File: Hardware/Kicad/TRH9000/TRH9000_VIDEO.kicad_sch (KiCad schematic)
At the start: 34 parts, among them J2 S-Video, J3 Composite, J4 DB15_Female_HighDensity, Q1 BC817, U6 CXA2075M

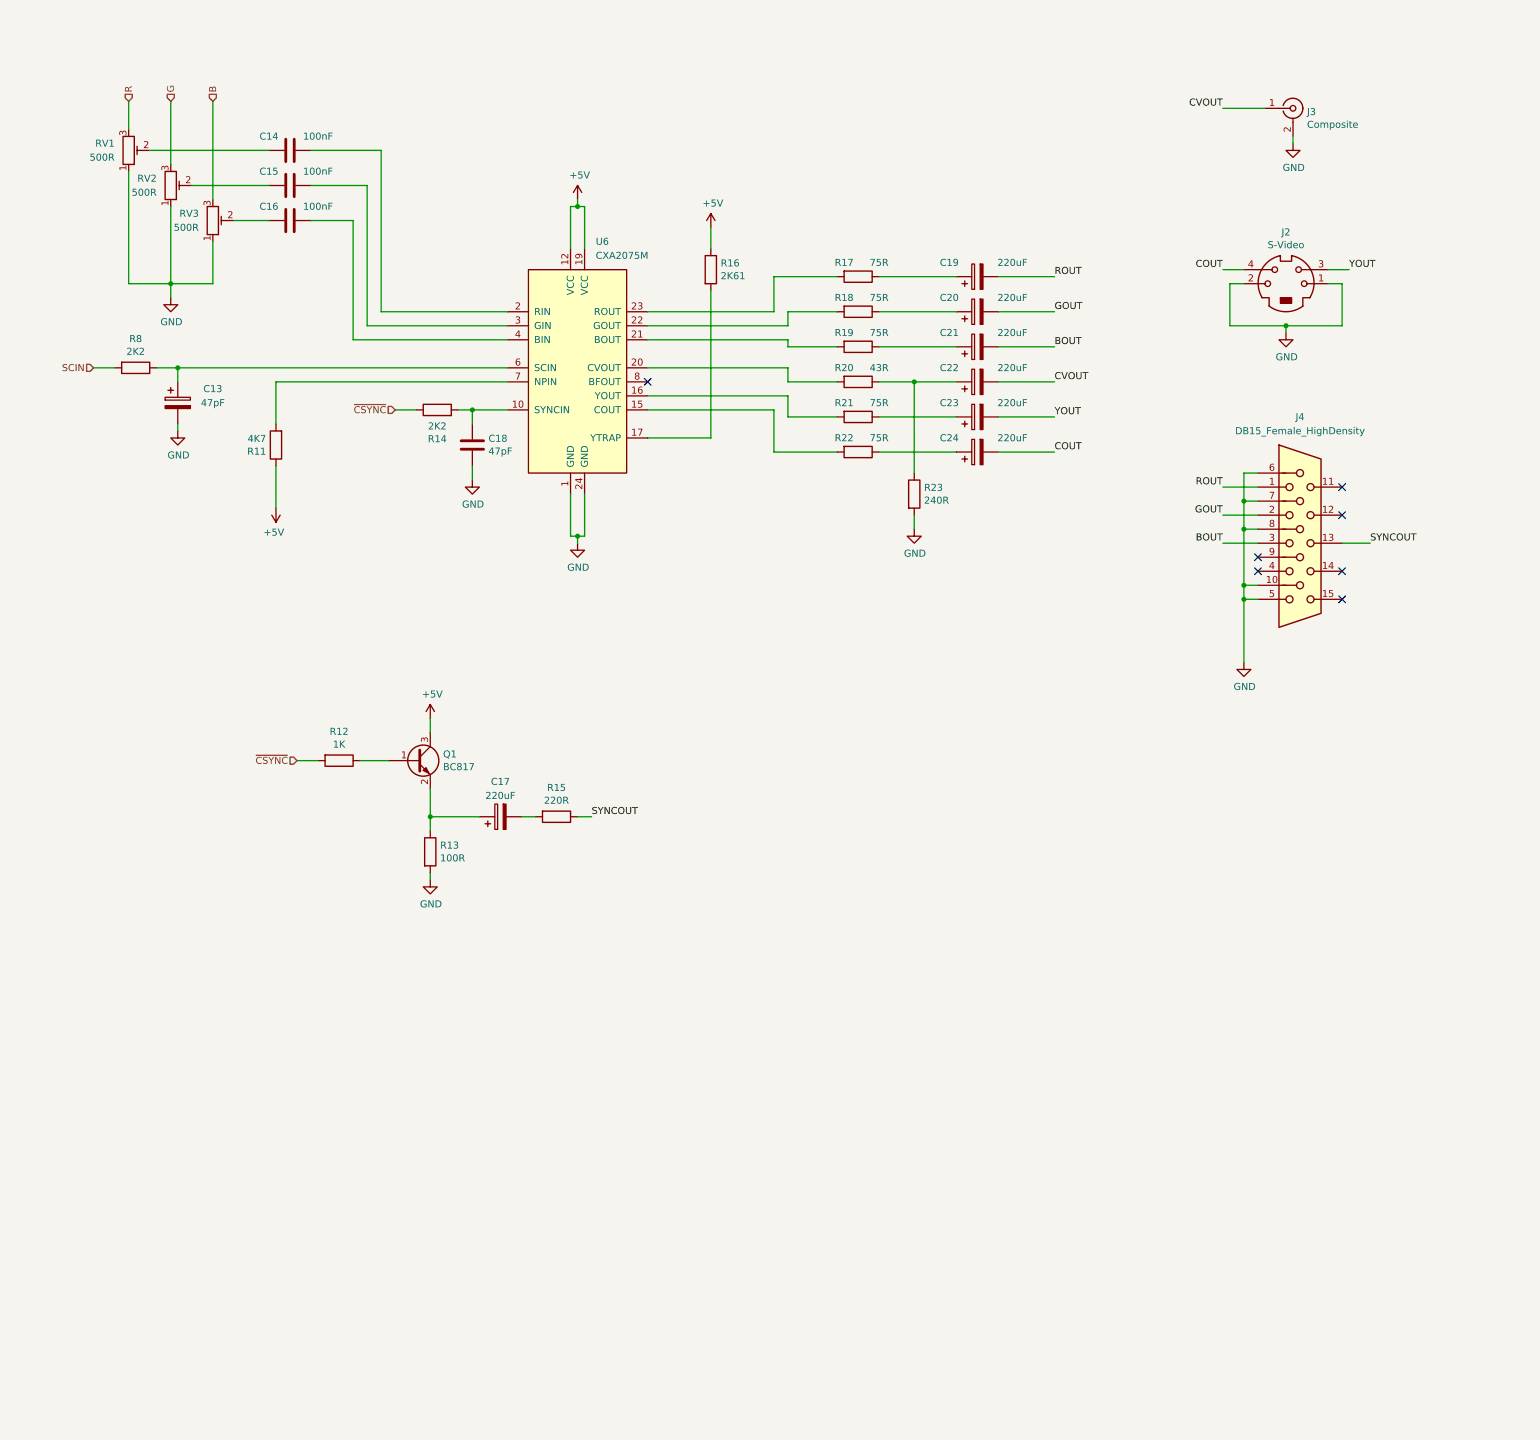
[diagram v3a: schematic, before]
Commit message: Footprint adjusts
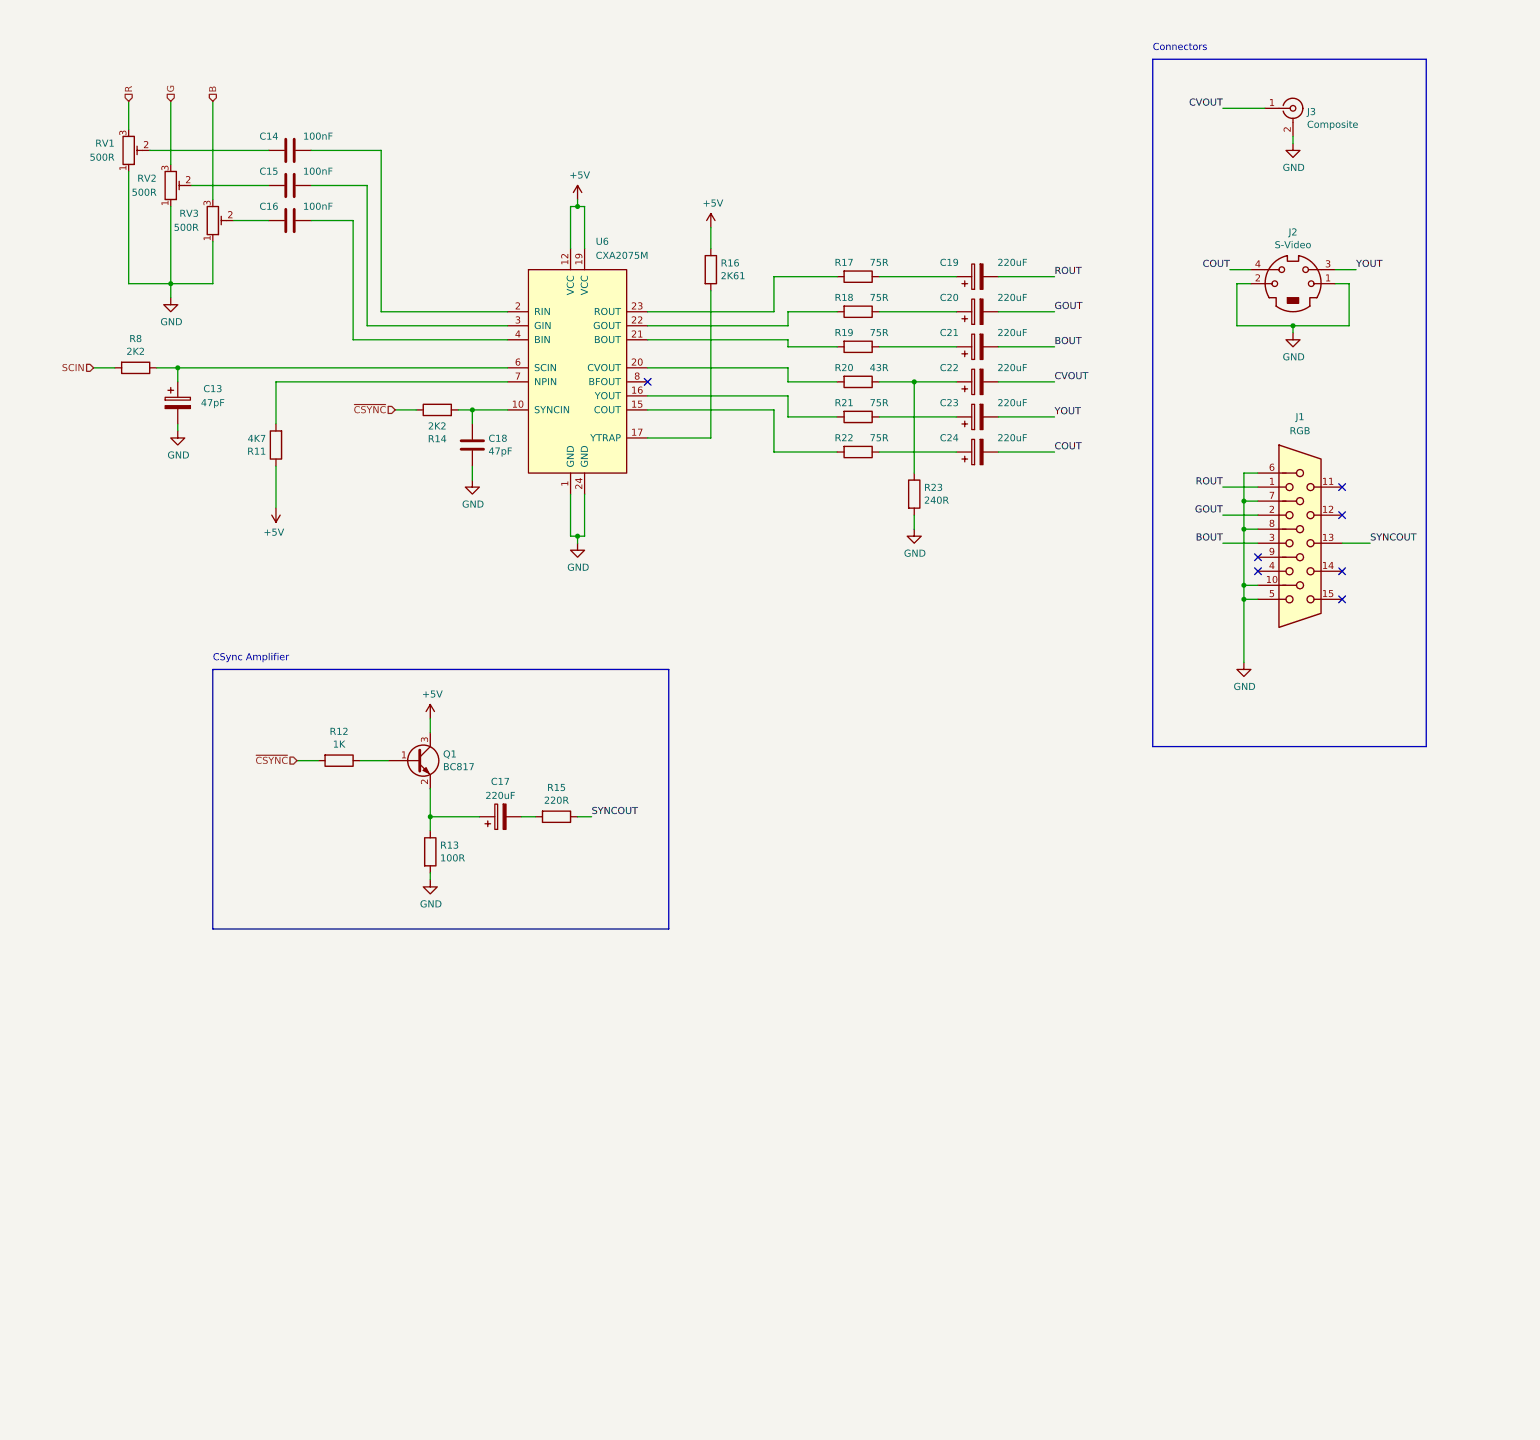
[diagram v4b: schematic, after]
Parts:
- J1: renamed from J4; value DB15_Female_HighDensity -> RGB
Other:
- note added: "CSync Amplifier"
- note added: "Connectors"
- moved on the sheet: J2
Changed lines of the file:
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@@
   (junction (at 45.72 78.74) (diameter 0) (color 0 0 0 0)
   )
-  (junction (at 246.38 71.12) (diameter 0) (color 0 0 0 0)
+  (junction (at 247.65 71.12) (diameter 0) (color 0 0 0 0)
   )
   (junction (at 179.07 81.28) (diameter 0) (color 0 0 0 0)
@@
     (stroke (width 0) (type default) (color 0 0 0 0))
   )
-  (wire (pts (xy 256.54 71.12) (xy 246.38 71.12))
+  (wire (pts (xy 257.81 71.12) (xy 247.65 71.12))
     (stroke (width 0) (type default) (color 0 0 0 0))
   )
@@
     (stroke (width 0) (type default) (color 0 0 0 0))
   )
-  (wire (pts (xy 236.22 71.12) (xy 236.22 63.5))
+  (wire (pts (xy 237.49 71.12) (xy 237.49 63.5))
     (stroke (width 0) (type default) (color 0 0 0 0))
   )
@@
     (stroke (width 0) (type default) (color 0 0 0 0))
   )
+  (polyline (pts (xy 52.07 133.35) (xy 134.62 133.35))
+    (stroke (width 0) (type default) (color 0 0 0 0))
+  )
   (wire (pts (xy 118.11 48.26) (xy 118.11 49.53))
     (stroke (width 0) (type default) (color 0 0 0 0))
   )
+  (polyline (pts (xy 134.62 133.35) (xy 134.62 180.34))
+    (stroke (width 0) (type default) (color 0 0 0 0))
+  )
   (wire (pts (xy 156.21 68.58) (xy 156.21 71.12))
     (stroke (width 0) (type default) (color 0 0 0 0))
@@
     (stroke (width 0) (type default) (color 0 0 0 0))
   )
+  (polyline (pts (xy 222.25 147.32) (xy 271.78 147.32))
+    (stroke (width 0) (type default) (color 0 0 0 0))
+  )
   (wire (pts (xy 96.52 86.36) (xy 99.06 86.36))
     (stroke (width 0) (type default) (color 0 0 0 0))
@@
     (stroke (width 0) (type default) (color 0 0 0 0))
   )
+  (polyline (pts (xy 134.62 180.34) (xy 52.07 180.34))
+    (stroke (width 0) (type default) (color 0 0 0 0))
+  )
   (wire (pts (xy 238.76 118.11) (xy 241.3 118.11))
     (stroke (width 0) (type default) (color 0 0 0 0))
@@
     (stroke (width 0) (type default) (color 0 0 0 0))
   )
-  (wire (pts (xy 236.22 63.5) (xy 238.76 63.5))
+  (wire (pts (xy 237.49 63.5) (xy 240.03 63.5))
     (stroke (width 0) (type default) (color 0 0 0 0))
   )
@@
     (stroke (width 0) (type default) (color 0 0 0 0))
   )
-  (wire (pts (xy 254 63.5) (xy 256.54 63.5))
+  (wire (pts (xy 255.27 63.5) (xy 257.81 63.5))
     (stroke (width 0) (type default) (color 0 0 0 0))
   )
@@
     (stroke (width 0) (type default) (color 0 0 0 0))
   )
-  (wire (pts (xy 238.76 60.96) (xy 234.95 60.96))
+  (wire (pts (xy 240.03 60.96) (xy 236.22 60.96))
     (stroke (width 0) (type default) (color 0 0 0 0))
   )
@@
     (stroke (width 0) (type default) (color 0 0 0 0))
   )
-  (wire (pts (xy 246.38 71.12) (xy 236.22 71.12))
+  (wire (pts (xy 247.65 71.12) (xy 237.49 71.12))
     (stroke (width 0) (type default) (color 0 0 0 0))
   )
@@
     (stroke (width 0) (type default) (color 0 0 0 0))
   )
-  (wire (pts (xy 246.38 72.39) (xy 246.38 71.12))
+  (wire (pts (xy 247.65 72.39) (xy 247.65 71.12))
     (stroke (width 0) (type default) (color 0 0 0 0))
   )
@@
     (stroke (width 0) (type default) (color 0 0 0 0))
   )
+  (polyline (pts (xy 52.07 133.35) (xy 52.07 180.34))
+    (stroke (width 0) (type default) (color 0 0 0 0))
+  )
   (wire (pts (xy 238.76 118.11) (xy 238.76 120.65))
     (stroke (width 0) (type default) (color 0 0 0 0))
@@
     (stroke (width 0) (type default) (color 0 0 0 0))
   )
-  (wire (pts (xy 256.54 63.5) (xy 256.54 71.12))
+  (wire (pts (xy 257.81 63.5) (xy 257.81 71.12))
     (stroke (width 0) (type default) (color 0 0 0 0))
   )
@@
     (stroke (width 0) (type default) (color 0 0 0 0))
   )
-  (wire (pts (xy 257.81 60.96) (xy 254 60.96))
+  (wire (pts (xy 259.08 60.96) (xy 255.27 60.96))
     (stroke (width 0) (type default) (color 0 0 0 0))
   )
@@
     (stroke (width 0) (type default) (color 0 0 0 0))
   )
+  (polyline (pts (xy 222.25 22.86) (xy 222.25 147.32))
+    (stroke (width 0) (type default) (color 0 0 0 0))
+  )
   (wire (pts (xy 36.83 43.18) (xy 36.83 63.5))
     (stroke (width 0) (type default) (color 0 0 0 0))
@@
     (stroke (width 0) (type default) (color 0 0 0 0))
   )
+  (polyline (pts (xy 271.78 147.32) (xy 271.78 22.86))
+    (stroke (width 0) (type default) (color 0 0 0 0))
+  )
+  (polyline (pts (xy 222.25 22.86) (xy 271.78 22.86))
+    (stroke (width 0) (type default) (color 0 0 0 0))
+  )
   (wire (pts (xy 156.21 83.82) (xy 156.21 87.63))
     (stroke (width 0) (type default) (color 0 0 0 0))
@@
   (wire (pts (xy 77.47 52.07) (xy 77.47 73.66))
     (stroke (width 0) (type default) (color 0 0 0 0))
+  )
+  (text "CSync Amplifier" (at 52.07 132.08 0)
+    (effects (font (size 1.27 1.27)) (justify left bottom))
+  )
+  (text "Connectors\n" (at 222.25 21.59 0)
+    (effects (font (size 1.27 1.27)) (justify left bottom))
   )
   (label "COUT" (at 204.47 93.98 0)
@@
     (effects (font (size 1.27 1.27)) (justify left bottom))
   )
-  (label "YOUT" (at 257.81 60.96 0)
+  (label "YOUT" (at 259.08 60.96 0)
     (effects (font (size 1.27 1.27)) (justify left bottom))
   )
@@
     (effects (font (size 1.27 1.27)) (justify right bottom))
   )
-  (label "COUT" (at 234.95 60.96 180)
+  (label "COUT" (at 236.22 60.96 180)
     (effects (font (size 1.27 1.27)) (justify right bottom))
   )
@@
     (pin "2")
   )
-  (symbol (lib_id "power:GND") (at 246.38 72.39 0) (unit 1)
-    (in_bom yes) (on_board yes)
-    (property "Reference" "#PWR0149" (id 0) (at 246.38 78.74 0)
-      (effects (font (size 1.27 1.27)) hide)
-    )
-    (property "Value" "GND" (id 1) (at 246.507 76.7842 0))
-    (property "Footprint" "" (id 2) (at 246.38 72.39 0)
-      (effects (font (size 1.27 1.27)) hide)
-    )
-    (property "Datasheet" "" (id 3) (at 246.38 72.39 0)
+  (symbol (lib_id "power:GND") (at 247.65 72.39 0) (unit 1)
+    (in_bom yes) (on_board yes)
+    (property "Reference" "#PWR0149" (id 0) (at 247.65 78.74 0)
+      (effects (font (size 1.27 1.27)) hide)
+    )
+    (property "Value" "GND" (id 1) (at 247.777 76.7842 0))
+    (property "Footprint" "" (id 2) (at 247.65 72.39 0)
+      (effects (font (size 1.27 1.27)) hide)
+    )
+    (property "Datasheet" "" (id 3) (at 247.65 72.39 0)
       (effects (font (size 1.27 1.27)) hide)
     )
@@
     (pin "2")
   )
-  (symbol (lib_id "Connector:Mini-DIN-4") (at 246.38 63.5 0) (unit 1)
-    (in_bom yes) (on_board yes)
-    (property "Reference" "J2" (id 0) (at 246.38 54.1782 0))
-    (property "Value" "S-Video" (id 1) (at 246.38 56.4896 0))
-    (property "Footprint" "trh9000:MINI-DIN-4-TE_5749181-1" (id 2) (at 246.38 63.5 0)
-      (effects (font (size 1.27 1.27)) hide)
-    )
-    (property "Datasheet" "http://service.powerdynamics.com/ec/Catalog17/Section%2011.pdf" (id 3) (at 246.38 63.5 0)
+  (symbol (lib_id "Connector:Mini-DIN-4") (at 247.65 63.5 0) (unit 1)
+    (in_bom yes) (on_board yes)
+    (property "Reference" "J2" (id 0) (at 247.65 54.1782 0))
+    (property "Value" "S-Video" (id 1) (at 247.65 56.4896 0))
+    (property "Footprint" "trh9000:MINI-DIN-4-TE_5749181-1" (id 2) (at 247.65 63.5 0)
+      (effects (font (size 1.27 1.27)) hide)
+    )
+    (property "Datasheet" "http://service.powerdynamics.com/ec/Catalog17/Section%2011.pdf" (id 3) (at 247.65 63.5 0)
       (effects (font (size 1.27 1.27)) hide)
     )
@@
   (symbol (lib_id "Connector:DB15_Female_HighDensity") (at 248.92 110.49 0) (unit 1)
     (in_bom yes) (on_board yes) (fields_autoplaced)
-    (property "Reference" "J4" (id 0) (at 248.92 87.63 0))
-    (property "Value" "DB15_Female_HighDensity" (id 1) (at 248.92 90.17 0))
+    (property "Reference" "J1" (id 0) (at 248.92 87.63 0))
+    (property "Value" "RGB" (id 1) (at 248.92 90.17 0))
     (property "Footprint" "Connector_Dsub:DSUB-15-HD_Female_Horizontal_P2.29x1.98mm_EdgePinOffset3.03mm_Housed_MountingHolesOffset4.94mm" (id 2) (at 224.79 100.33 0)
       (effects (font (size 1.27 1.27)) hide)

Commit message: Initial component placement on the PCB.
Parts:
- J2: footprint trh9000:MINI-DIN-4-TE_5749181-1 -> Connector_PinHeader_2.54mm:PinHeader_1x04_P2.54mm_Vertical
- J3: footprint trh9000:KLPX0848A2RG -> Connector_PinHeader_1.00mm:PinHeader_1x02_P1.00mm_Vertical
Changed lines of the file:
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@@
   (title_block
     (title "TRH9000")
-    (date "2022-08-02")
-    (rev "1")
+    (date "2022-08-04")
+    (rev "0")
     (company "The Retro Hacker")
     (comment 2 "Shared under CERN-OHL-S license")
@@
       (effects (font (size 1.27 1.27)) (justify left))
     )
-    (property "Footprint" "trh9000:KLPX0848A2RG" (id 2) (at 247.65 31.75 0)
+    (property "Footprint" "Connector_PinHeader_1.00mm:PinHeader_1x02_P1.00mm_Vertical" (id 2) (at 247.65 31.75 0)
       (effects (font (size 1.27 1.27)) hide)
     )
@@
     (property "Reference" "J2" (id 0) (at 247.65 54.1782 0))
     (property "Value" "S-Video" (id 1) (at 247.65 56.4896 0))
-    (property "Footprint" "trh9000:MINI-DIN-4-TE_5749181-1" (id 2) (at 247.65 63.5 0)
-      (effects (font (size 1.27 1.27)) hide)
-    )
+    (property "Footprint" "Connector_PinHeader_2.54mm:PinHeader_1x04_P2.54mm_Vertical" (id 2) (at 247.65 63.5 0)
+      (effects (font (size 1.27 1.27)) hide)
+    )

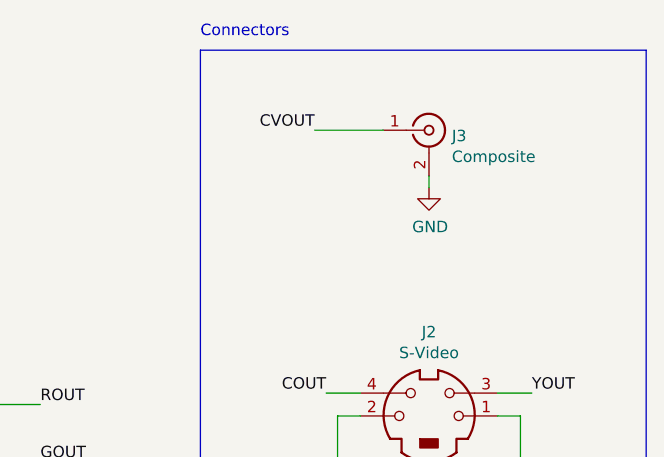
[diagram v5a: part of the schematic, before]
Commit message: Routing 1. First 3d view of the current PCB.
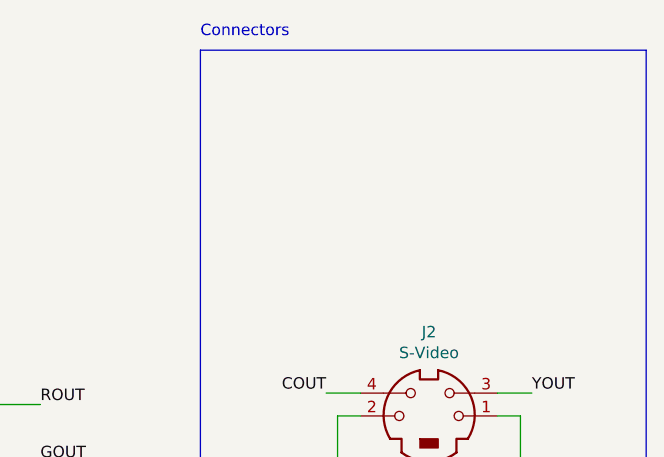
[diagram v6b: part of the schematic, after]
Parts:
- removed J3: Composite, Connector_PinHeader_1.00mm:PinHeader_1x02_P1.00mm_Vertical, symbol Connector:Conn_Coaxial
- R8: footprint Resistor_SMD:R_0815_2038Metric -> Resistor_SMD:R_0805_2012Metric
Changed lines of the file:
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@@
-    (stroke (width 0) (type default) (color 0 0 0 0))
-  )
-  (wire (pts (xy 234.95 31.75) (xy 242.57 31.75))
     (stroke (width 0) (type default) (color 0 0 0 0))
   )
@@
   )
   (wire (pts (xy 179.07 107.95) (xy 179.07 105.41))
-    (stroke (width 0) (type default) (color 0 0 0 0))
-  )
-  (wire (pts (xy 247.65 38.1) (xy 247.65 36.83))
     (stroke (width 0) (type default) (color 0 0 0 0))
   )
@@
     (effects (font (size 1.27 1.27)) (justify right bottom))
   )
-  (label "CVOUT" (at 234.95 31.75 180)
-    (effects (font (size 1.27 1.27)) (justify right bottom))
-  )
   (label "SYNCOUT" (at 261.62 110.49 0)
     (effects (font (size 1.27 1.27)) (justify left bottom))
@@
   (hierarchical_label "R" (shape input) (at 36.83 30.48 90)
     (effects (font (size 1.27 1.27)) (justify left))
-  )
-  (symbol (lib_id "power:GND") (at 247.65 38.1 0) (unit 1)
-    (in_bom yes) (on_board yes)
-    (property "Reference" "#PWR0148" (id 0) (at 247.65 44.45 0)
-      (effects (font (size 1.27 1.27)) hide)
-    )
-    (property "Value" "GND" (id 1) (at 247.777 42.4942 0))
-    (property "Footprint" "" (id 2) (at 247.65 38.1 0)
-      (effects (font (size 1.27 1.27)) hide)
-    )
-    (property "Datasheet" "" (id 3) (at 247.65 38.1 0)
-      (effects (font (size 1.27 1.27)) hide)
-    )
-    (pin "1")
   )
   (symbol (lib_id "Device:R") (at 168.91 87.63 270) (unit 1)
@@
     )
     (pin "1")
-  )
-  (symbol (lib_id "Connector:Conn_Coaxial") (at 247.65 31.75 0) (unit 1)
-    (in_bom yes) (on_board yes)
-    (property "Reference" "J3" (id 0) (at 250.19 32.385 0)
-      (effects (font (size 1.27 1.27)) (justify left))
-    )
-    (property "Value" "Composite" (id 1) (at 250.19 34.6964 0)
-      (effects (font (size 1.27 1.27)) (justify left))
-    )
-    (property "Footprint" "Connector_PinHeader_1.00mm:PinHeader_1x02_P1.00mm_Vertical" (id 2) (at 247.65 31.75 0)
-      (effects (font (size 1.27 1.27)) hide)
-    )
-    (property "Datasheet" " ~" (id 3) (at 247.65 31.75 0)
-      (effects (font (size 1.27 1.27)) hide)
-    )
-    (pin "1")
-    (pin "2")
   )
   (symbol (lib_id "Connector:Mini-DIN-4") (at 247.65 63.5 0) (unit 1)
@@
     (property "Reference" "R8" (id 0) (at 38.1 73.4822 90))
     (property "Value" "2K2" (id 1) (at 38.1 75.7936 90))
-    (property "Footprint" "Resistor_SMD:R_0815_2038Metric" (id 2) (at 38.1 76.962 90)
-      (effects (font (size 1.27 1.27)) hide)
-    )
+    (property "Footprint" "Resistor_SMD:R_0805_2012Metric" (id 2) (at 38.1 76.962 90)
+      (effects (font (size 1.27 1.27)) hide)
+    )
